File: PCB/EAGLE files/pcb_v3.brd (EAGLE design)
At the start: 100 x 80 mm, 10 parts

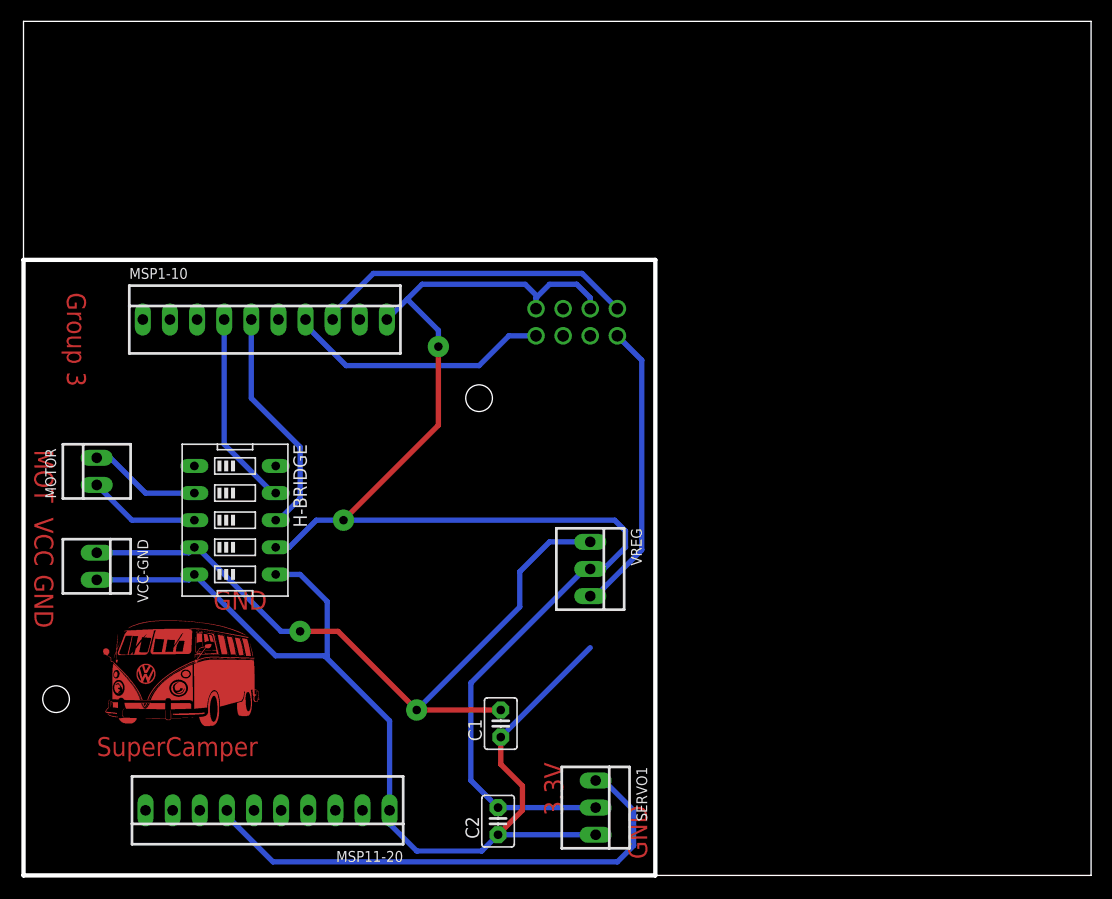
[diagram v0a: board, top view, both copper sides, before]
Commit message: PCB with new VR ready for print
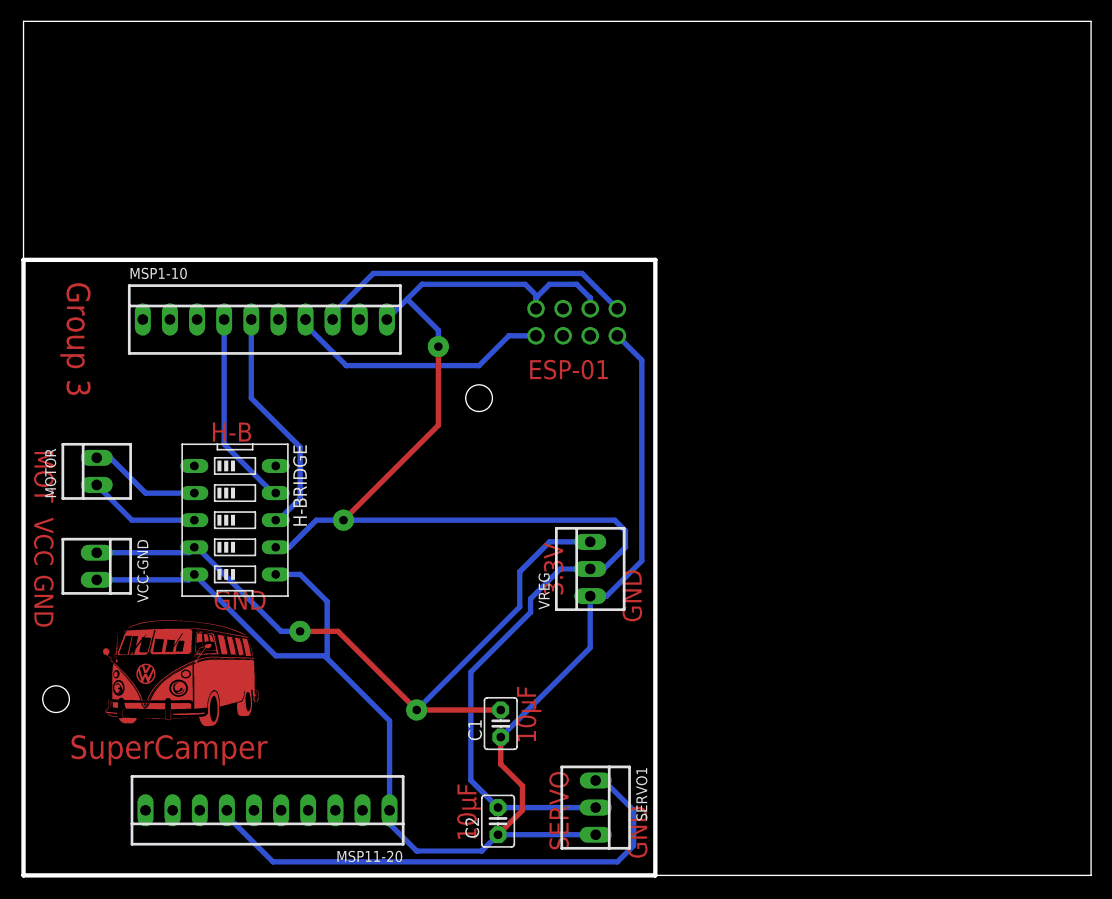
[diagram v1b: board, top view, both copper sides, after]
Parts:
- turned VREG to 90 degrees
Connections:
- net N$12: now also VREG.1; no longer VREG.2
- net N$14: now also VREG.3; no longer VREG.1
- net N$4: now also VREG.2; no longer VREG.3
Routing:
- net N$12: track 125.6 -> 131.5 mm
- net N$4: track 125.6 -> 128.7 mm
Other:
- board text added: "10µF"
- board text added: "ESP-01"
- board text added: "H-B"
- board text added: "SERVO"
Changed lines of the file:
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@@
 <rectangle x1="12.7127" y1="23.8633" x2="14.3891" y2="23.8887" layer="1"/>
 <text x="0" y="-0.127" size="0.0508" layer="21" font="vector">C:/Users/mrdav/Desktop/EE579/SuperCamper/PCB/Logo2.bmp</text>
-<text x="4.064" y="54.61" size="1.778" layer="1" font="vector" rot="SR270">Group 3</text>
+<text x="4.064" y="55.626" size="2.1844" layer="1" font="vector" rot="SR270">Group 3</text>
 <text x="1.016" y="39.878" size="1.778" layer="1" font="vector" rot="SR270">MOT</text>
-<text x="6.858" y="11.176" size="1.778" layer="1" font="vector">SuperCamper</text>
-<text x="50.546" y="5.588" size="1.778" layer="1" font="vector" rot="R90">3.3V</text>
+<text x="4.318" y="10.922" size="2.1844" layer="1" font="vector">SuperCamper</text>
+<text x="50.546" y="26.162" size="1.778" layer="1" font="vector" rot="R90">3.3V</text>
 <text x="17.78" y="24.892" size="1.778" layer="1" font="vector">GND</text>
+<text x="56.134" y="28.702" size="1.778" layer="1" font="vector" rot="R270">GND</text>
+<text x="47.244" y="46.482" size="1.778" layer="1" font="vector">ESP-01</text>
+<text x="51.054" y="2.286" size="1.778" layer="1" font="vector" rot="R90">SERVO</text>
+<text x="17.526" y="40.64" size="1.778" layer="1" font="vector">H-B</text>
+<text x="40.64" y="8.636" size="1.778" layer="1" font="vector" rot="R270">10µF</text>
+<text x="46.228" y="17.78" size="1.778" layer="1" font="vector" rot="R270">10µF</text>
 </plain>
 <attributes>
@@
 <attribute name="OC_NEWARK" value="25C3832" x="6.858" y="28.956" size="1.778" layer="27" rot="R270" display="off"/>
 </element>
-<element name="VREG" library="con-molex" package="22-23-2031" value="3.3V" x="53.086" y="28.702" rot="R270">
-<attribute name="MF" value="MOLEX" x="53.086" y="28.702" size="1.778" layer="27" rot="R270" display="off"/>
-<attribute name="MPN" value="22-23-2031" x="53.086" y="28.702" size="1.778" layer="27" rot="R270" display="off"/>
-<attribute name="OC_FARNELL" value="1462950" x="53.086" y="28.702" size="1.778" layer="27" rot="R270" display="off"/>
-<attribute name="OC_NEWARK" value="30C0862" x="53.086" y="28.702" size="1.778" layer="27" rot="R270" display="off"/>
+<element name="VREG" library="con-molex" package="22-23-2031" value="3.3V" x="53.086" y="28.702" rot="R90">
+<attribute name="MF" value="MOLEX" x="53.086" y="28.702" size="1.778" layer="27" rot="R90" display="off"/>
+<attribute name="MPN" value="22-23-2031" x="53.086" y="28.702" size="1.778" layer="27" rot="R90" display="off"/>
+<attribute name="OC_FARNELL" value="1462950" x="53.086" y="28.702" size="1.778" layer="27" rot="R90" display="off"/>
+<attribute name="OC_NEWARK" value="30C0862" x="53.086" y="28.702" size="1.778" layer="27" rot="R90" display="off"/>
 </element>
 </elements>
@@
 <wire x1="24.892" y1="30.734" x2="27.432" y2="33.274" width="0.5" layer="16"/>
 <wire x1="23.622" y1="30.734" x2="24.892" y2="30.734" width="0.5" layer="16"/>
-<wire x1="41.91" y1="8.89" x2="41.91" y2="18.034" width="0.5" layer="16"/>
+<wire x1="41.91" y1="8.89" x2="41.91" y2="19.05" width="0.5" layer="16"/>
 <wire x1="44.45" y1="6.35" x2="41.91" y2="8.89" width="0.5" layer="16"/>
 <wire x1="29.972" y1="33.274" x2="29.972" y2="33.02" width="0.5" layer="16"/>
@@
 <wire x1="27.432" y1="33.274" x2="29.972" y2="33.274" width="0.5" layer="16"/>
 <wire x1="55.372" y1="33.274" x2="29.972" y2="33.274" width="0.5" layer="16"/>
-<wire x1="41.91" y1="18.034" x2="52.578" y2="28.702" width="0.5" layer="16"/>
-<wire x1="54.356" y1="28.702" x2="56.388" y2="30.734" width="0.5" layer="16"/>
 <wire x1="56.388" y1="30.734" x2="56.388" y2="32.258" width="0.5" layer="16"/>
 <wire x1="56.388" y1="32.258" x2="55.372" y2="33.274" width="0.5" layer="16"/>
-<contactref element="VREG" pad="3"/>
-<wire x1="52.578" y1="28.702" x2="54.356" y2="28.702" width="0" layer="19" extent="16-16"/>
-<wire x1="53.086" y1="26.162" x2="41.91" y2="8.89" width="0" layer="19" extent="16-16"/>
+<contactref element="VREG" pad="2"/>
+<wire x1="54.356" y1="28.702" x2="56.388" y2="30.734" width="0.5" layer="16"/>
+<wire x1="53.086" y1="28.702" x2="54.356" y2="28.702" width="0.5" layer="16"/>
+<wire x1="53.086" y1="28.702" x2="50.292" y2="28.702" width="0.5" layer="16"/>
+<wire x1="47.498" y1="24.638" x2="41.91" y2="19.05" width="0.5" layer="16"/>
+<wire x1="47.498" y1="25.908" x2="47.498" y2="24.638" width="0.5" layer="16"/>
+<wire x1="50.292" y1="28.702" x2="47.498" y2="25.908" width="0.5" layer="16"/>
 </signal>
 <signal name="N$2">
@@
 <wire x1="46.736" y1="6.096" x2="46.736" y2="8.382" width="0.5" layer="1"/>
 <wire x1="44.45" y1="3.81" x2="46.736" y2="6.096" width="0.5" layer="1"/>
-<wire x1="57.912" y1="30.48" x2="53.594" y2="26.162" width="0.5" layer="16"/>
-<wire x1="57.912" y1="48.26" x2="57.912" y2="30.48" width="0.5" layer="16"/>
+<wire x1="57.912" y1="48.26" x2="57.912" y2="29.464" width="0.5" layer="16"/>
 <wire x1="55.626" y1="50.546" x2="57.912" y2="48.26" width="0.5" layer="16"/>
 <wire x1="53.086" y1="21.336" x2="44.704" y2="12.954" width="0.5" layer="16"/>
-<contactref element="VREG" pad="2"/>
-<wire x1="53.086" y1="21.336" x2="53.594" y2="26.162" width="0" layer="19" extent="16-16"/>
-<wire x1="53.086" y1="28.702" x2="34.29" y2="4.826" width="0" layer="19" extent="16-16"/>
+<contactref element="VREG" pad="1"/>
+<wire x1="53.086" y1="21.336" x2="53.086" y2="26.162" width="0.5" layer="16"/>
+<wire x1="54.61" y1="26.162" x2="57.912" y2="29.464" width="0.5" layer="16"/>
+<wire x1="53.086" y1="26.162" x2="54.61" y2="26.162" width="0.5" layer="16"/>
 </signal>
 <signal name="N$14">
@@
 <wire x1="36.83" y1="15.494" x2="46.482" y2="25.146" width="0.5" layer="16"/>
 <wire x1="46.482" y1="28.448" x2="49.276" y2="31.242" width="0.5" layer="16"/>
-<contactref element="VREG" pad="1"/>
+<contactref element="VREG" pad="3"/>
 <wire x1="49.276" y1="31.242" x2="53.086" y2="31.242" width="0.5" layer="16"/>
 </signal>

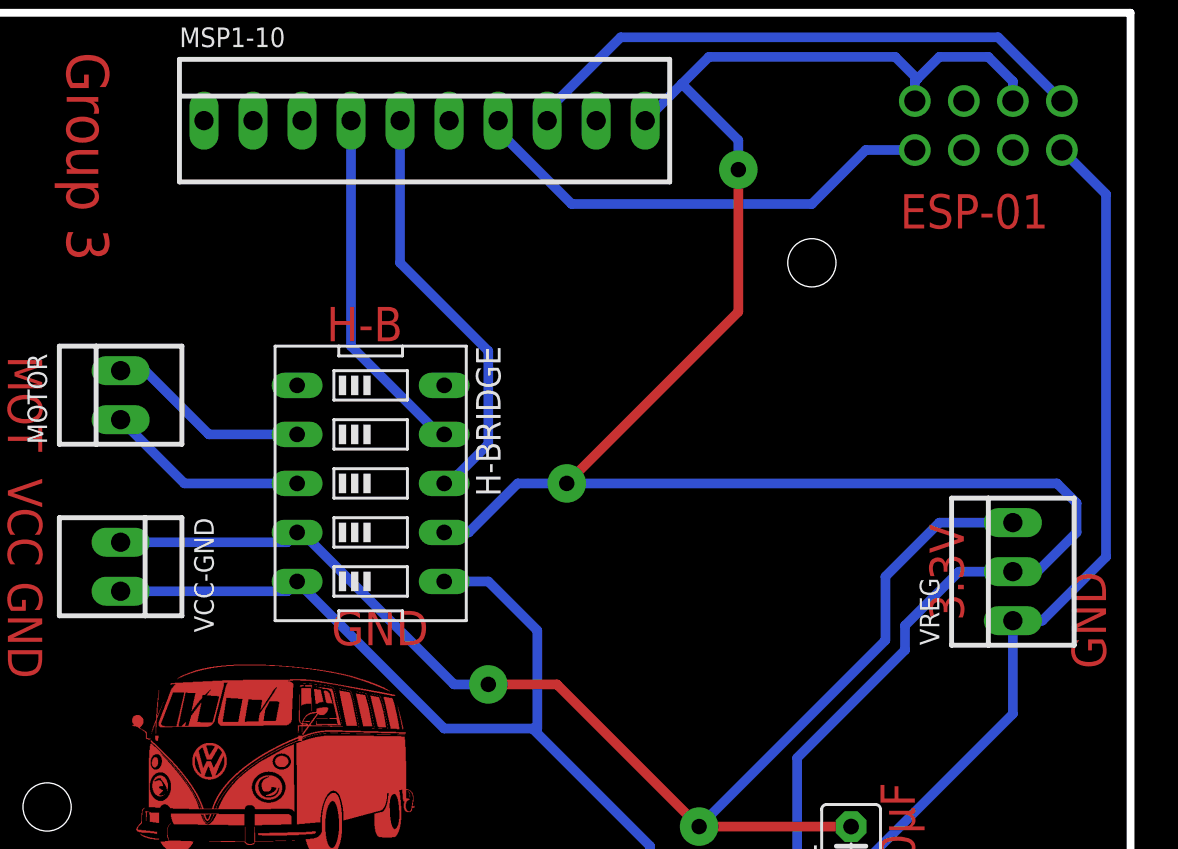
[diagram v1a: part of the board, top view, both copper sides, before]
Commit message: Add second ESP8266 to PCB
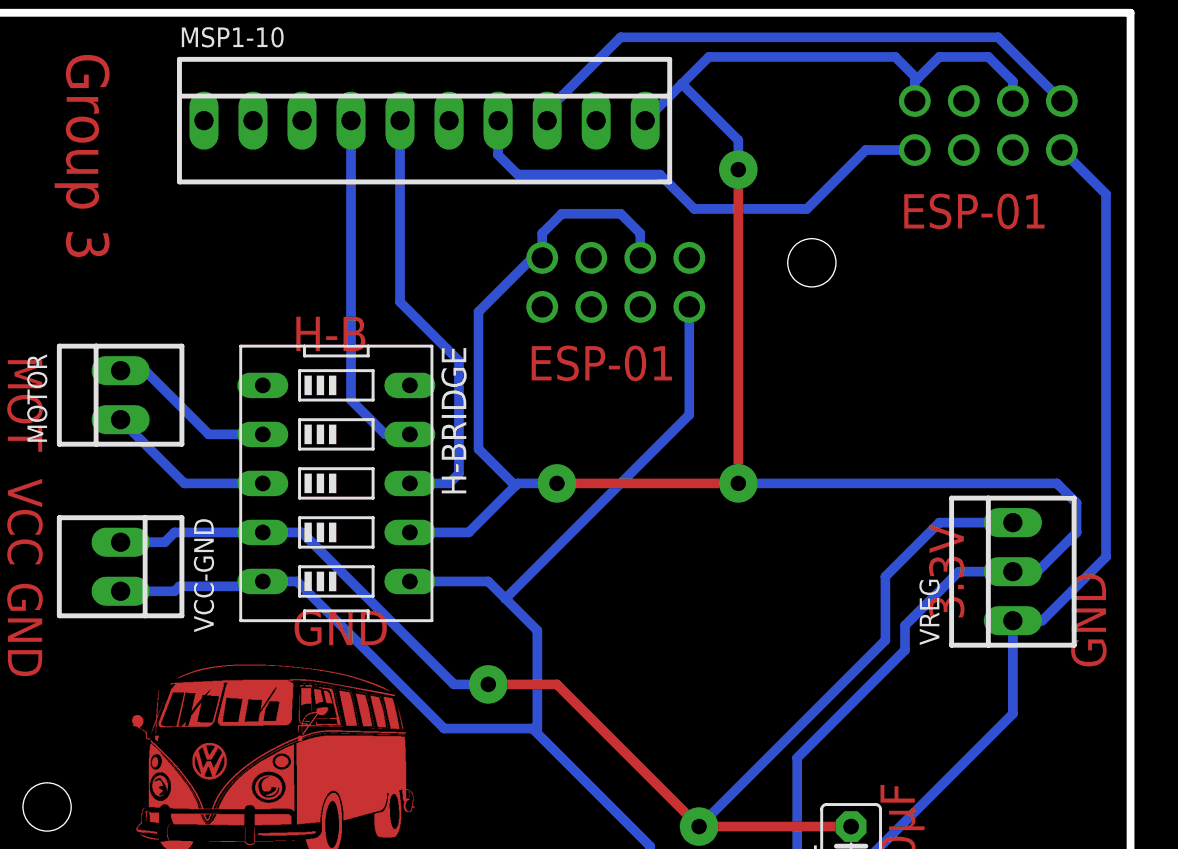
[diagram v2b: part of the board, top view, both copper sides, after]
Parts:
- added J2: (no value), Board-to-Board (rev17e):61300821121
- moved H-BRIDGE 1.78 mm to (18.0, 33.3)
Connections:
- net N$12: now also J2.8
- net N$4: now also J2.1, J2.5
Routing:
- net N$4: track 128.7 -> 149.4 mm, vias 2 -> 3
- net N$12: track 131.5 -> 152.2 mm
- net N$5: track 10.5 -> 8.73 mm
- net N$6: track 10.5 -> 8.73 mm
- net N$1: track 24.8 -> 25.8 mm
- net N$11: track 21.8 -> 22.3 mm
